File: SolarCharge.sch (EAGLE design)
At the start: 15 parts, among them U1 TINY4/5/9/10-TSHR/TS8R

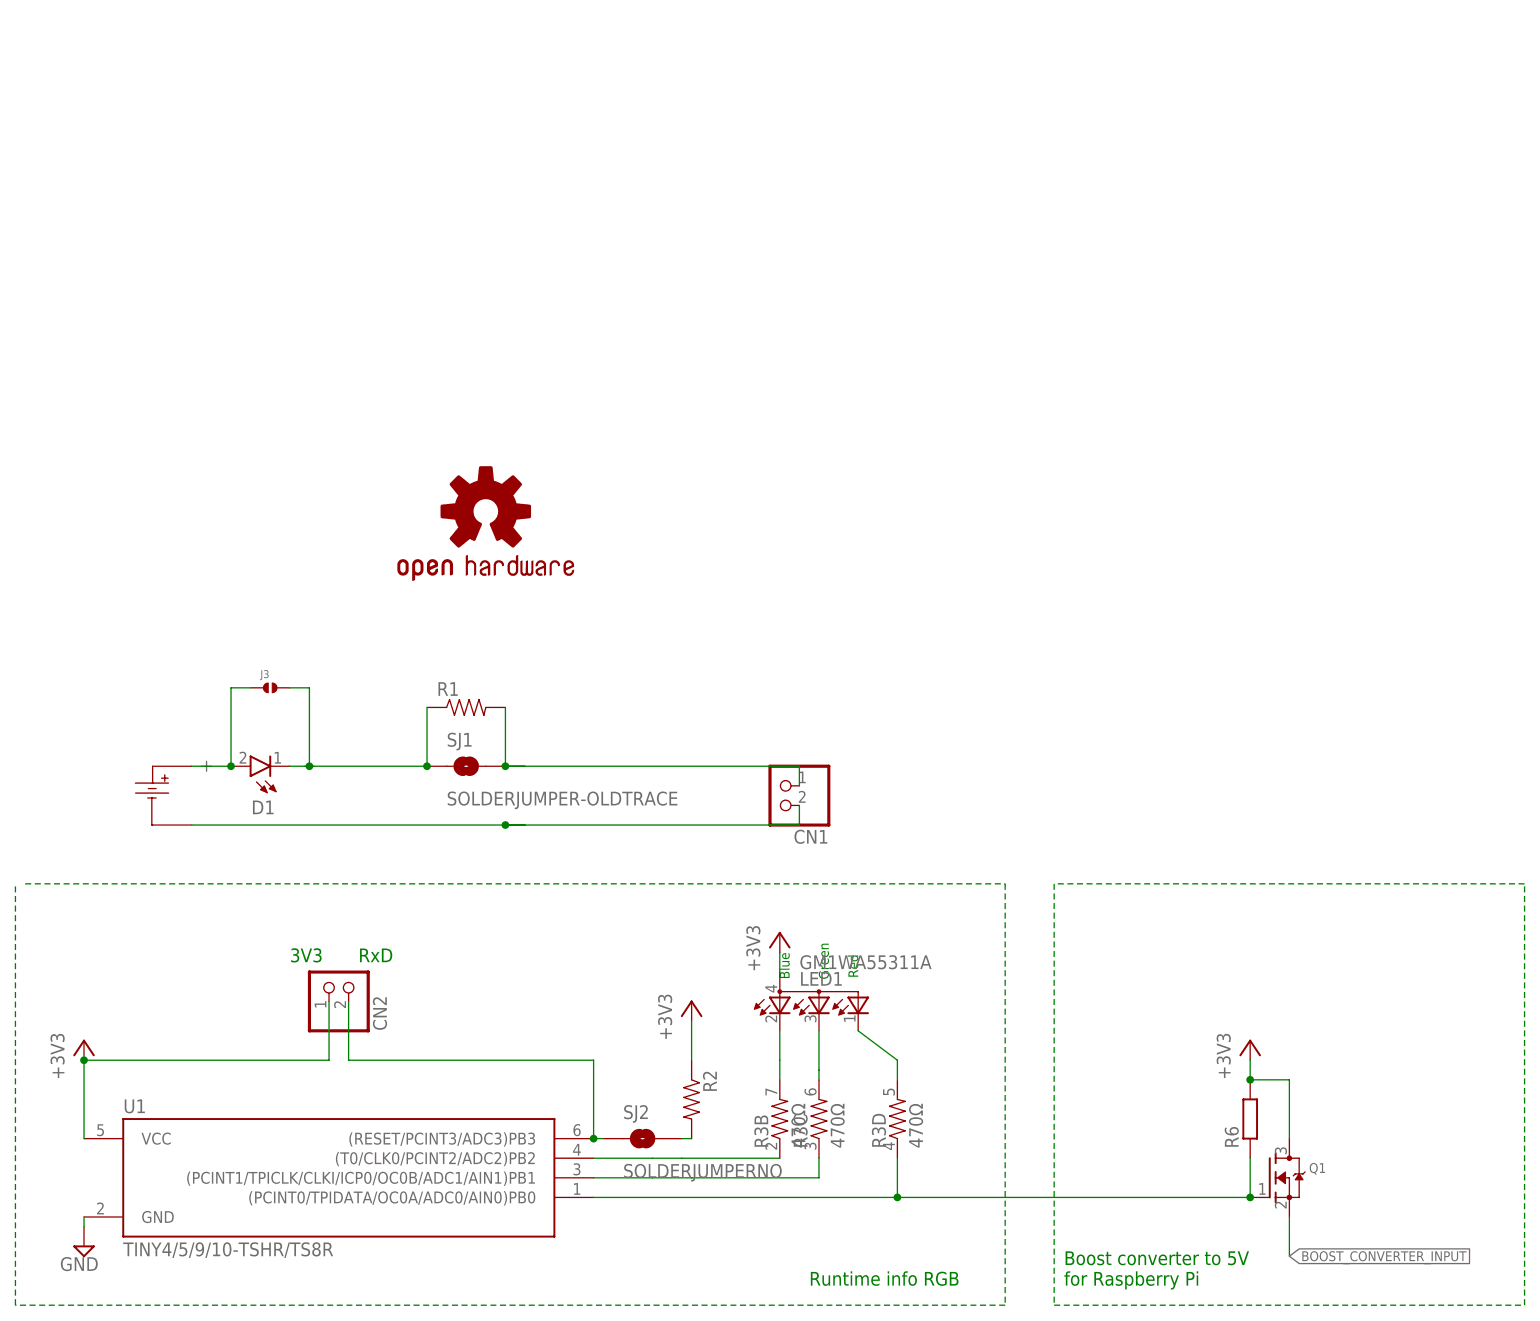
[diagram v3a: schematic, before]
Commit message: Add overvoltage protection
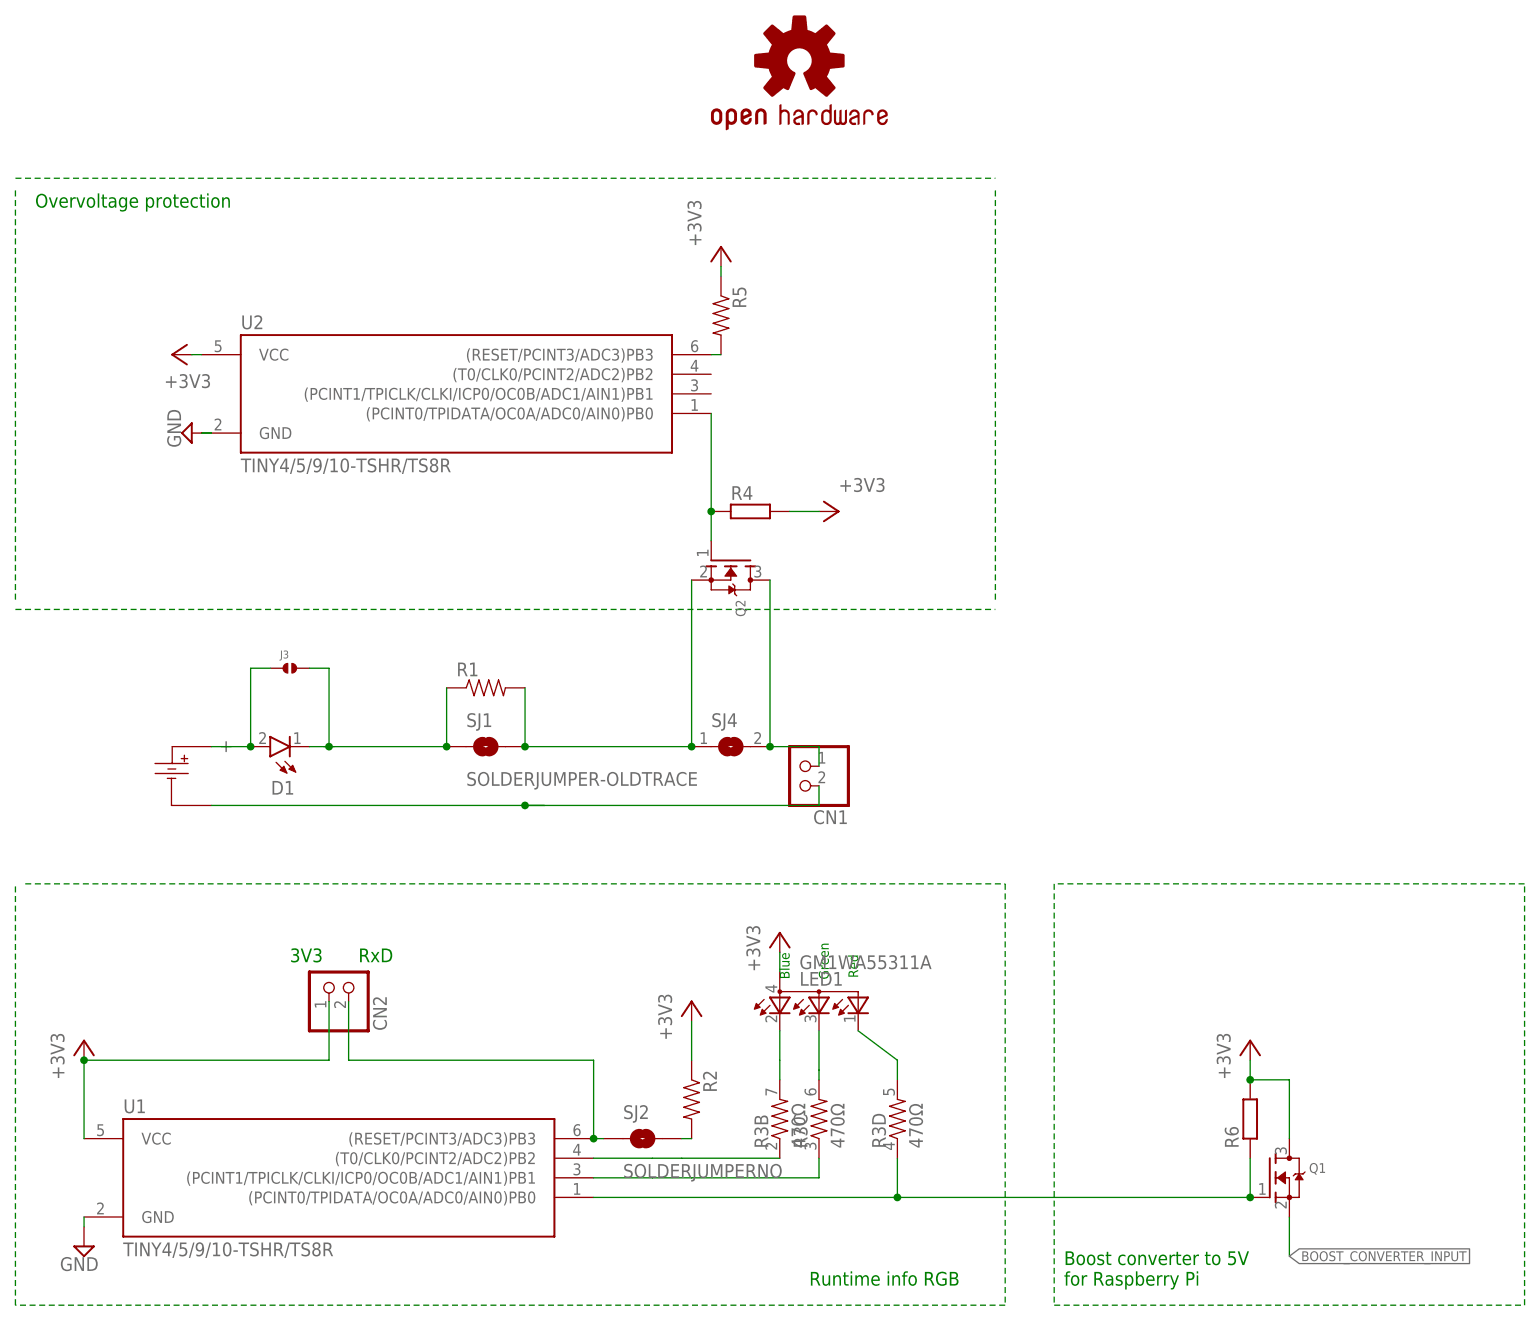
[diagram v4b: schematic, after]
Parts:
- added Q2: (no value), adafruit:MOSFET-NREFLOW
- added R4: (no value), rcl:R-EU_R0603
- added R5: (no value), ROHM:RESISTOR0603-RES
- added SJ4: (no value), jumper:SJ
- added U2: TINY4/5/9/10-TSHR/TS8R, bt_avr:TINY4/5/9/10-TSHR/TS8R
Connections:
- new net N$10: Q2.G, R4.1, U2.(PCINT0/TPIDATA/OC0A/ADC0/AIN0)PB0
- new net N$11: R5.2, U2.(RESET/PCINT3/ADC3)PB3
- new net N$9: CN1.2, Q2.D, SJ4.2
- net +3V3: now also R4.2, R5.1, U2.VCC
- net GND: now also U2.GND
- net N$4: now also Q2.S, SJ4.1; no longer CN1.2
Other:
- note added: "Overvoltage protection"
- moved on the sheet: CN1, D1, J3, R1, SJ1
